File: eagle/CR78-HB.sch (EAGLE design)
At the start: 34 parts, among them Q1 2N3904, Q2 2N3904, Q3 2N3904, X1 22-23-2021

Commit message: lb
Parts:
- C2: value 8n2 -> 12n
- C3: value 8n2 -> 18n
- C4: value 6n8 -> 12n
- C5: value 6n8 -> 10n
- C6: value 2n2 -> 8n2
- R14: value 1M5 -> 680k
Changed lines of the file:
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@@
 <part name="R6" library="rcl" deviceset="R-US_" device="0207/7" value="56k"/>
 <part name="R5" library="rcl" deviceset="R-US_" device="0207/7" value="15k"/>
-<part name="C2" library="rcl" deviceset="C-US" device="050-025X075" value="8n2"/>
-<part name="C3" library="rcl" deviceset="C-US" device="050-025X075" value="8n2"/>
-<part name="C4" library="rcl" deviceset="C-US" device="050-025X075" value="6n8"/>
+<part name="C2" library="rcl" deviceset="C-US" device="050-025X075" value="12n"/>
+<part name="C3" library="rcl" deviceset="C-US" device="050-025X075" value="18n"/>
+<part name="C4" library="rcl" deviceset="C-US" device="050-025X075" value="12n"/>
 <part name="R8" library="rcl" deviceset="R-US_" device="0207/7" value="10k"/>
 <part name="R7" library="TR808clone" deviceset="TRIM_EU-" device="B64Y" value="10KB"/>
-<part name="C5" library="rcl" deviceset="C-US" device="050-025X075" value="6n8"/>
+<part name="C5" library="rcl" deviceset="C-US" device="050-025X075" value="10n"/>
 <part name="R9" library="rcl" deviceset="R-US_" device="0207/7" value="15k"/>
 <part name="Q2" library="808_lt" deviceset="2N3904" device=""/>
@@
 <part name="R10" library="rcl" deviceset="R-US_" device="0207/7" value="1M5"/>
 <part name="R11" library="rcl" deviceset="R-US_" device="0207/7" value="10k"/>
-<part name="R14" library="rcl" deviceset="R-US_" device="0207/7" value="1M5"/>
-<part name="C6" library="rcl" deviceset="C-US" device="050-025X075" value="2n2"/>
+<part name="R14" library="rcl" deviceset="R-US_" device="0207/7" value="680k"/>
+<part name="C6" library="rcl" deviceset="C-US" device="050-025X075" value="8n2"/>
 <part name="R12" library="TR808clone" deviceset="TRIM_EU-" device="B64Y" value="500R"/>
 <part name="GND4" library="supply1" deviceset="GND" device=""/>

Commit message: lc
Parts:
- C2, C4: value 12n -> 22n
- C3: value 18n -> 27n
- C5: value 10n -> 22n
- C6: value 8n2 -> 10n
- R14: value 680k -> 560k
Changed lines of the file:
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@@
 <part name="R6" library="rcl" deviceset="R-US_" device="0207/7" value="56k"/>
 <part name="R5" library="rcl" deviceset="R-US_" device="0207/7" value="15k"/>
-<part name="C2" library="rcl" deviceset="C-US" device="050-025X075" value="12n"/>
-<part name="C3" library="rcl" deviceset="C-US" device="050-025X075" value="18n"/>
-<part name="C4" library="rcl" deviceset="C-US" device="050-025X075" value="12n"/>
+<part name="C2" library="rcl" deviceset="C-US" device="050-025X075" value="22n"/>
+<part name="C3" library="rcl" deviceset="C-US" device="050-025X075" value="27n"/>
+<part name="C4" library="rcl" deviceset="C-US" device="050-025X075" value="22n"/>
 <part name="R8" library="rcl" deviceset="R-US_" device="0207/7" value="10k"/>
 <part name="R7" library="TR808clone" deviceset="TRIM_EU-" device="B64Y" value="10KB"/>
-<part name="C5" library="rcl" deviceset="C-US" device="050-025X075" value="10n"/>
+<part name="C5" library="rcl" deviceset="C-US" device="050-025X075" value="22n"/>
 <part name="R9" library="rcl" deviceset="R-US_" device="0207/7" value="15k"/>
 <part name="Q2" library="808_lt" deviceset="2N3904" device=""/>
@@
 <part name="R10" library="rcl" deviceset="R-US_" device="0207/7" value="1M5"/>
 <part name="R11" library="rcl" deviceset="R-US_" device="0207/7" value="10k"/>
-<part name="R14" library="rcl" deviceset="R-US_" device="0207/7" value="680k"/>
-<part name="C6" library="rcl" deviceset="C-US" device="050-025X075" value="8n2"/>
+<part name="R14" library="rcl" deviceset="R-US_" device="0207/7" value="560k"/>
+<part name="C6" library="rcl" deviceset="C-US" device="050-025X075" value="10n"/>
 <part name="R12" library="TR808clone" deviceset="TRIM_EU-" device="B64Y" value="500R"/>
 <part name="GND4" library="supply1" deviceset="GND" device=""/>

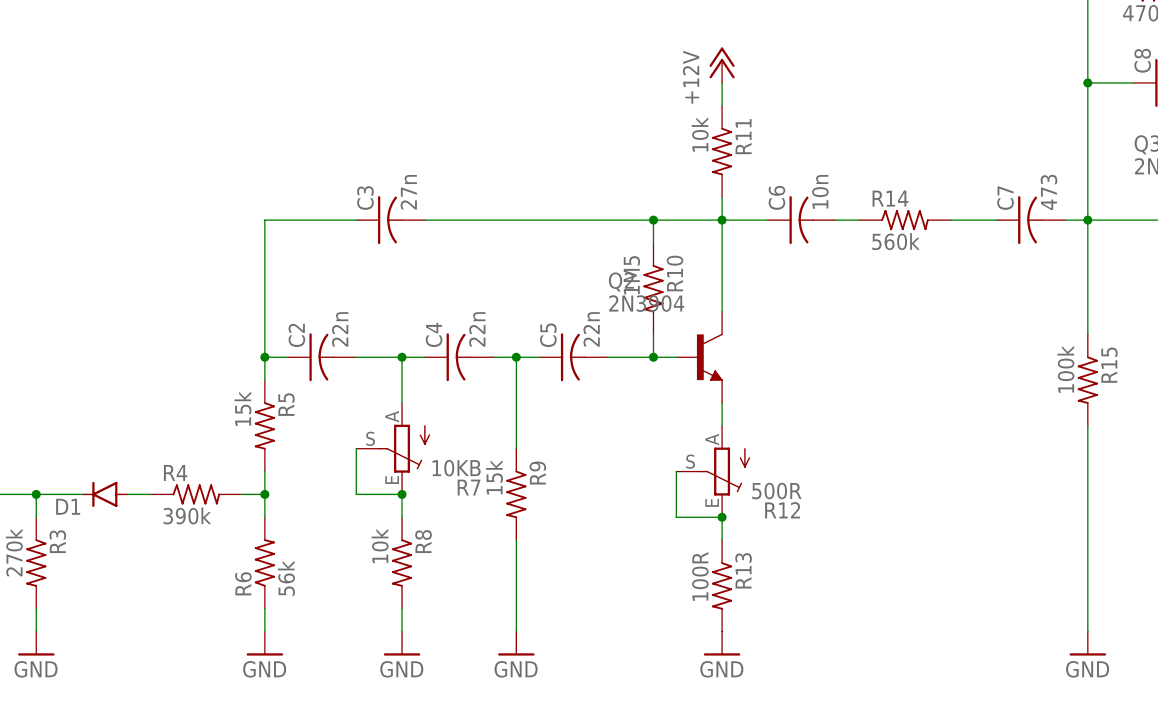
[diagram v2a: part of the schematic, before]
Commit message: added output pulldown 10k for bd
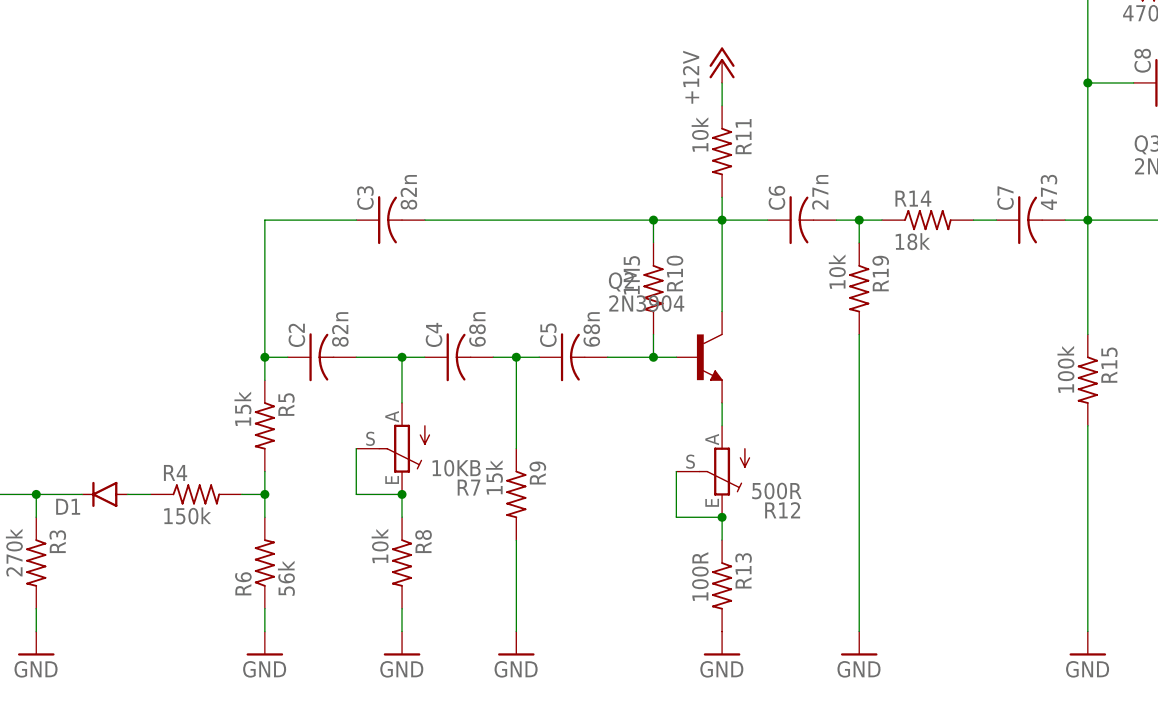
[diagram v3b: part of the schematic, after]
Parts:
- added R19: 10k, rcl:R-US_0207/2V
- C2: value 22n -> 82n
- C3: value 27n -> 82n
- C4, C5: value 22n -> 68n
- C6: value 10n -> 27n
- R14: value 560k -> 18k
- R18: device rcl:R-US_0207/7 -> rcl:R-US_0207/2V
- R4: value 390k -> 150k
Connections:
- net GND: now also R19.2
- net N$14: now also R19.1
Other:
- moved on the sheet: R14
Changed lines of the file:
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@@
 <part name="D1" library="SparkFun-DiscreteSemi" deviceset="DIODE" device="1N4148"/>
 <part name="GND3" library="supply1" deviceset="GND" device=""/>
-<part name="R4" library="rcl" deviceset="R-US_" device="0207/7" value="390k"/>
+<part name="R4" library="rcl" deviceset="R-US_" device="0207/7" value="150k"/>
 <part name="R6" library="rcl" deviceset="R-US_" device="0207/7" value="56k"/>
 <part name="R5" library="rcl" deviceset="R-US_" device="0207/7" value="15k"/>
-<part name="C2" library="rcl" deviceset="C-US" device="050-025X075" value="22n"/>
-<part name="C3" library="rcl" deviceset="C-US" device="050-025X075" value="27n"/>
-<part name="C4" library="rcl" deviceset="C-US" device="050-025X075" value="22n"/>
+<part name="C2" library="rcl" deviceset="C-US" device="050-025X075" value="82n"/>
+<part name="C3" library="rcl" deviceset="C-US" device="050-025X075" value="82n"/>
+<part name="C4" library="rcl" deviceset="C-US" device="050-025X075" value="68n"/>
 <part name="R8" library="rcl" deviceset="R-US_" device="0207/7" value="10k"/>
 <part name="R7" library="TR808clone" deviceset="TRIM_EU-" device="B64Y" value="10KB"/>
-<part name="C5" library="rcl" deviceset="C-US" device="050-025X075" value="22n"/>
+<part name="C5" library="rcl" deviceset="C-US" device="050-025X075" value="68n"/>
 <part name="R9" library="rcl" deviceset="R-US_" device="0207/7" value="15k"/>
 <part name="Q2" library="808_lt" deviceset="2N3904" device=""/>
@@
 <part name="R10" library="rcl" deviceset="R-US_" device="0207/7" value="1M5"/>
 <part name="R11" library="rcl" deviceset="R-US_" device="0207/7" value="10k"/>
-<part name="R14" library="rcl" deviceset="R-US_" device="0207/7" value="560k"/>
-<part name="C6" library="rcl" deviceset="C-US" device="050-025X075" value="10n"/>
+<part name="R14" library="rcl" deviceset="R-US_" device="0207/7" value="18k"/>
+<part name="C6" library="rcl" deviceset="C-US" device="050-025X075" value="27n"/>
 <part name="R12" library="TR808clone" deviceset="TRIM_EU-" device="B64Y" value="500R"/>
 <part name="GND4" library="supply1" deviceset="GND" device=""/>
@@
 <part name="R16" library="rcl" deviceset="R-US_" device="0207/7" value="470k"/>
 <part name="R17" library="rcl" deviceset="R-US_" device="0207/7" value="47k"/>
-<part name="R18" library="rcl" deviceset="R-US_" device="0207/7" value="220R"/>
+<part name="R18" library="rcl" deviceset="R-US_" device="0207/2V" value="220R"/>
 <part name="C9" library="rcl" deviceset="CPOL-US" device="B45181A" value="1uF"/>
 <part name="JCK1" library="erthenvar" deviceset="AUDIO-JACK" device=""/>
@@
 <part name="R15" library="rcl" deviceset="R-US_" device="0207/7" value="100k"/>
 <part name="GND8" library="supply1" deviceset="GND" device=""/>
+<part name="R19" library="rcl" deviceset="R-US_" device="0207/2V" value="10k"/>
+<part name="GND12" library="supply1" deviceset="GND" device=""/>
 </parts>
 <sheets>
@@
 <instance part="R10" gate="G$1" x="111.76" y="71.12" rot="R270"/>
 <instance part="R11" gate="G$1" x="119.38" y="86.36" rot="R270"/>
-<instance part="R14" gate="G$1" x="139.7" y="78.74"/>
+<instance part="R14" gate="G$1" x="142.24" y="78.74"/>
 <instance part="C6" gate="G$1" x="127" y="78.74" rot="R90"/>
 <instance part="R12" gate="1" x="119.38" y="50.8" smashed="yes" rot="R180">
@@
 <instance part="R15" gate="G$1" x="160.02" y="60.96" rot="R270"/>
 <instance part="GND8" gate="1" x="160.02" y="30.48"/>
+<instance part="R19" gate="G$1" x="134.62" y="71.12" rot="R270"/>
+<instance part="GND12" gate="1" x="134.62" y="30.48"/>
 </instances>
 <busses>
@@
 <pinref part="GND8" gate="1" pin="GND"/>
 <wire x1="160.02" y1="33.02" x2="160.02" y2="55.88" width="0.1524" layer="91"/>
+</segment>
+<segment>
+<pinref part="R19" gate="G$1" pin="2"/>
+<pinref part="GND12" gate="1" pin="GND"/>
+<wire x1="134.62" y1="33.02" x2="134.62" y2="66.04" width="0.1524" layer="91"/>
 </segment>
 </net>
@@
 <pinref part="R14" gate="G$1" pin="1"/>
 <pinref part="C6" gate="G$1" pin="2"/>
+<wire x1="137.16" y1="78.74" x2="134.62" y2="78.74" width="0.1524" layer="91"/>
+<pinref part="R19" gate="G$1" pin="1"/>
 <wire x1="134.62" y1="78.74" x2="132.08" y2="78.74" width="0.1524" layer="91"/>
+<wire x1="134.62" y1="76.2" x2="134.62" y2="78.74" width="0.1524" layer="91"/>
+<junction x="134.62" y="78.74"/>
 </segment>
 </net>
@@
 <pinref part="R14" gate="G$1" pin="2"/>
 <pinref part="C7" gate="G$1" pin="1"/>
-<wire x1="144.78" y1="78.74" x2="149.86" y2="78.74" width="0.1524" layer="91"/>
-</segment>
-</net>
+<wire x1="147.32" y1="78.74" x2="149.86" y2="78.74" width="0.1524" layer="91"/>
+</segment>
+</net>
